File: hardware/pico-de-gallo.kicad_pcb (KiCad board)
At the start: 2 copper layers, 50 x 69.5 mm, 14 parts, among them J1 Conn_02x08_Odd_Even, J2 Conn_01x02, J3 Conn_01x04, J4 Conn_01x05, J5 Conn_01x02, J6 Conn_01x03, J7 Conn_02x05_Odd_Even

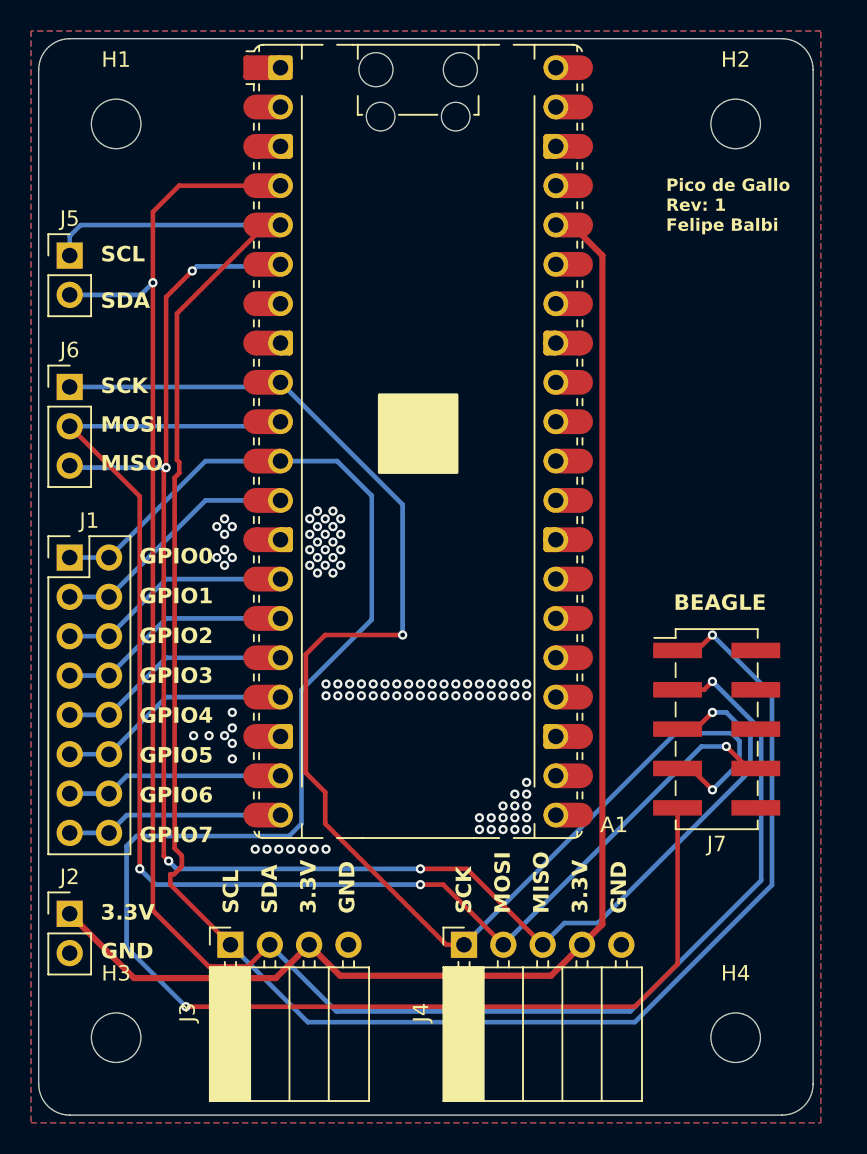
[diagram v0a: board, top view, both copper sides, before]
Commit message: hardware: change board stack-up
Make it a four layer PCB instead. While at that, also add ODP's logo.

Signed-off-by: Felipe Balbi <febalbi@microsoft.com>
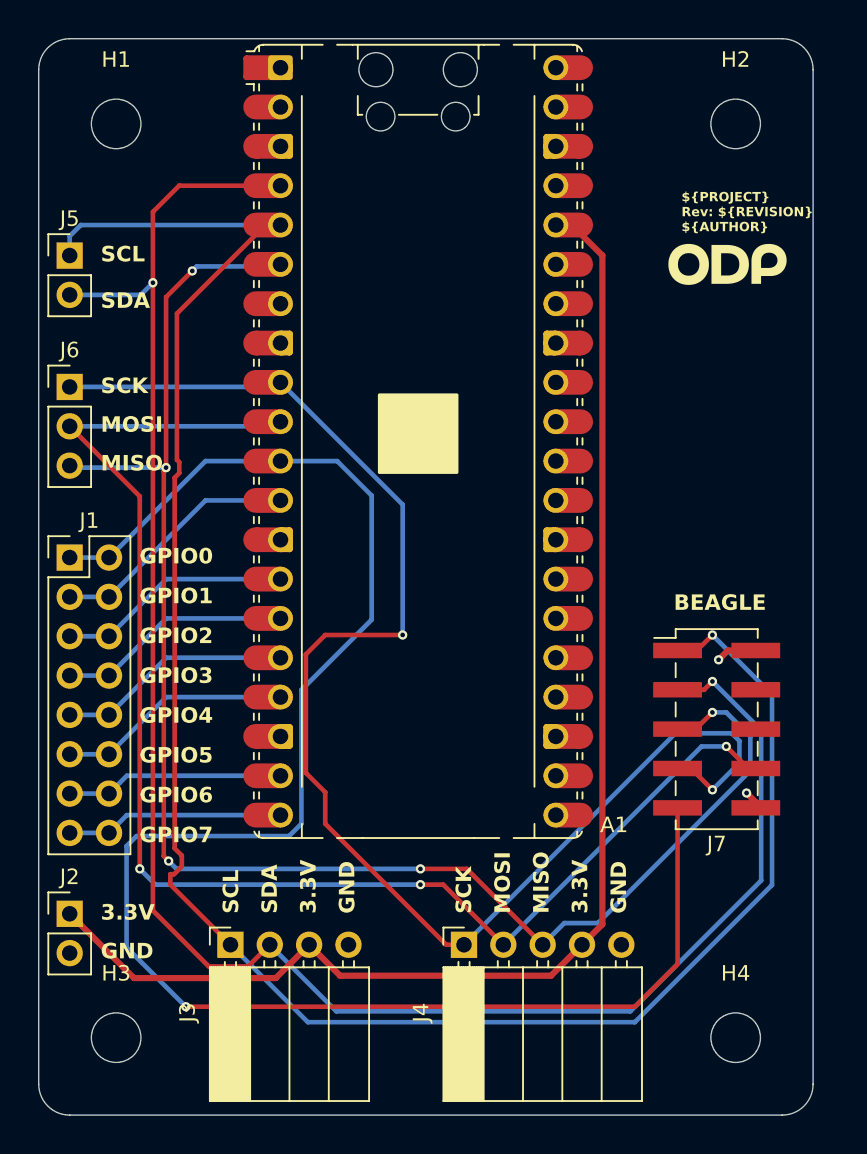
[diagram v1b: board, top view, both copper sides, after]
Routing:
- net GND: track 1.28 -> 6.95 mm, vias 96 -> 2
- added copper zone on In2.Cu, net +3V3
- added copper zone on In1.Cu, net GND
- removed copper zone on B.Cu, net GND
- removed copper zone on F.Cu, net GND
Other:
- copper layers 2 -> 4
- board text added: "${PROJECT} Rev: ${REVISION} ${AUTHOR}"
- board text removed: "Pico de Gallo Rev: 1 Felipe Balbi"
